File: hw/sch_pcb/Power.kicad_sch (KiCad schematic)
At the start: 32 parts

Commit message: Edit
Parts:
- removed ?: (no value), symbol Device:CP
- added C77, C79, C80: 47uF/6,3V, Mlab_R:SMD-0805, symbol Device:C
- added C81, C82: 100nF, Mlab_R:SMD-0805, symbol Device:C
- C67: renamed from ?; value (none) -> 10uF; footprint (none) -> Mlab_R:SMD-0805; Hodnota 10uF -> (none); Odkaz C31 -> (none); Pouzdro Mlab_R:SMD-0805 -> (none)
- C68: renamed from ?; value (none) -> 10uF; footprint (none) -> Mlab_R:SMD-0805; Hodnota 10uF -> (none); Odkaz C32 -> (none); Pouzdro Mlab_R:SMD-0805 -> (none)
- C69: renamed from ?; value (none) -> 100nF; footprint (none) -> Mlab_R:SMD-0805; Hodnota 100nF -> (none); Odkaz C33 -> (none); Pouzdro Mlab_R:SMD-0805 -> (none)
- C70: renamed from ?; value (none) -> 100nF; footprint (none) -> Mlab_R:SMD-0805; Hodnota 100nF -> (none); Odkaz C34 -> (none); Pouzdro Mlab_R:SMD-0805 -> (none)
- C71: renamed from ?; value (none) -> 100nF; footprint (none) -> Mlab_R:SMD-0805; Hodnota 100nF -> (none); Odkaz C35 -> (none); Pouzdro Mlab_R:SMD-0805 -> (none)
- C72: renamed from ?; value (none) -> 100nF; footprint (none) -> Mlab_R:SMD-0805; Hodnota 100nF -> (none); Odkaz C36 -> (none); Pouzdro Mlab_R:SMD-0805 -> (none)
- C73: renamed from ?; value (none) -> 10uF; footprint (none) -> Mlab_R:SMD-0805; Hodnota 10uF -> (none); Odkaz C37 -> (none); Pouzdro Mlab_R:SMD-0805 -> (none)
- C74: renamed from ?; value (none) -> 10uF; footprint (none) -> Mlab_R:SMD-0805; Hodnota 10uF -> (none); Odkaz C38 -> (none); Pouzdro Mlab_R:SMD-0805 -> (none)
- C75: renamed from ?; value (none) -> 10uF; footprint (none) -> Mlab_R:SMD-0805; Hodnota 10uF -> (none); Odkaz C39 -> (none); Pouzdro Mlab_R:SMD-0805 -> (none)
- C76: renamed from ?; value (none) -> 10uF; footprint (none) -> Mlab_R:SMD-0805; Hodnota 10uF -> (none); Odkaz C40 -> (none); Pouzdro Mlab_R:SMD-0805 -> (none)
- C78: renamed from ?; value (none) -> 47uF/16; footprint (none) -> Mlab_C:TantalC_SizeC_Reflow; Hodnota 47uF/16 -> (none); Odkaz C42 -> (none); Pouzdro Mlab_C:TantalC_SizeC_Reflow -> (none)
- D2: renamed from ?; value (none) -> RED; footprint (none) -> Mlab_D:LED_1206; Hodnota RED -> (none); Odkaz D2 -> (none); Pouzdro Mlab_D:LED_1206 -> (none)
- D3: renamed from ?; value (none) -> RED; footprint (none) -> Mlab_D:LED_1206; Hodnota RED -> (none); Odkaz D3 -> (none); Pouzdro Mlab_D:LED_1206 -> (none)
- L48: renamed from ?; value (none) -> 1uH; footprint (none) -> Mlab_L:DE1205-10; Hodnota 1uH -> (none); Odkaz L8 -> (none); Pouzdro Mlab_L:DE1205-10 -> (none)
- L49: renamed from ?; value (none) -> 1uH; footprint (none) -> Mlab_L:DE1205-10; Hodnota 1uH -> (none); Odkaz L9 -> (none); Pouzdro Mlab_L:DE1205-10 -> (none)
- L50: renamed from ?; value (none) -> BLM21PG331SN1D; Hodnota BLM21PG331SN1D -> (none); Odkaz L10 -> (none)
- L51: renamed from ?; value (none) -> BLM21PG331SN1D; Hodnota BLM21PG331SN1D -> (none); Odkaz L11 -> (none)
- R43: renamed from ?; value (none) -> 100k; footprint (none) -> Mlab_R:SMD-0805; Hodnota 100k -> (none); Odkaz R30 -> (none); Pouzdro Mlab_R:SMD-0805 -> (none)
- R44: renamed from ?; value (none) -> -; footprint (none) -> Mlab_R:SMD-0805; Hodnota - -> (none); Odkaz R31 -> (none); Pouzdro Mlab_R:SMD-0805 -> (none)
- R45: renamed from ?; value (none) -> 100k; footprint (none) -> Mlab_R:SMD-0805; Hodnota 100k -> (none); Odkaz R32 -> (none); Pouzdro Mlab_R:SMD-0805 -> (none)
- R46: renamed from ?; value (none) -> -; footprint (none) -> Mlab_R:SMD-0805; Hodnota - -> (none); Odkaz R33 -> (none); Pouzdro Mlab_R:SMD-0805 -> (none)
- R47: renamed from ?; value (none) -> 10k; footprint (none) -> Mlab_R:SMD-0805; Hodnota 10k -> (none); Odkaz R34 -> (none); Pouzdro Mlab_R:SMD-0805 -> (none)
- R48: renamed from ?; value (none) -> 10k; footprint (none) -> Mlab_R:SMD-0805; Hodnota 10k -> (none); Odkaz R35 -> (none); Pouzdro Mlab_R:SMD-0805 -> (none)
- R49: renamed from ?; value (none) -> 0R; footprint (none) -> Mlab_R:SMD-0805; Hodnota 0R -> (none); Odkaz R36 -> (none); Pouzdro Mlab_R:SMD-0805 -> (none)
- R50: renamed from ?; value (none) -> 0R; footprint (none) -> Mlab_R:SMD-0805; Hodnota 0R -> (none); Odkaz R37 -> (none); Pouzdro Mlab_R:SMD-0805 -> (none)
- R51: renamed from ?; value (none) -> 45k3; footprint (none) -> Mlab_R:SMD-0805; Hodnota 45k3 -> (none); Odkaz R38 -> (none); Pouzdro Mlab_R:SMD-0805 -> (none)
- R52: renamed from ?; value (none) -> 73k2; footprint (none) -> Mlab_R:SMD-0805; Hodnota 73k2 -> (none); Odkaz R39 -> (none); Pouzdro Mlab_R:SMD-0805 -> (none)
- R53: renamed from ?; value (none) -> 240R; footprint (none) -> Mlab_R:SMD-0805; Hodnota 240R -> (none); Odkaz R40 -> (none); Pouzdro Mlab_R:SMD-0805 -> (none)
- R54: renamed from ?; value (none) -> 240R; footprint (none) -> Mlab_R:SMD-0805; Hodnota 240R -> (none); Odkaz R41 -> (none); Pouzdro Mlab_R:SMD-0805 -> (none)
- U10: renamed from ?; value (none) -> TPS563249; footprint (none) -> Package_TO_SOT_SMD:SOT-23-6; Hodnota TPS563249 -> (none); Odkaz U6 -> (none); Pouzdro Package_TO_SOT_SMD:SOT-23-6 -> (none)
- U11: renamed from ?; value (none) -> TPS563249; footprint (none) -> Package_TO_SOT_SMD:SOT-23-6; Hodnota TPS563249 -> (none); Odkaz U7 -> (none); Pouzdro Package_TO_SOT_SMD:SOT-23-6 -> (none)
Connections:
- net +3V3: now also C79.2, C81.2
- net +5V: now also C80.2, C82.2
- net GND: now also C77.1, C79.1, C80.1, C81.1, C82.1
- net at C73.2, C75.2, L48.2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: now also C77.2

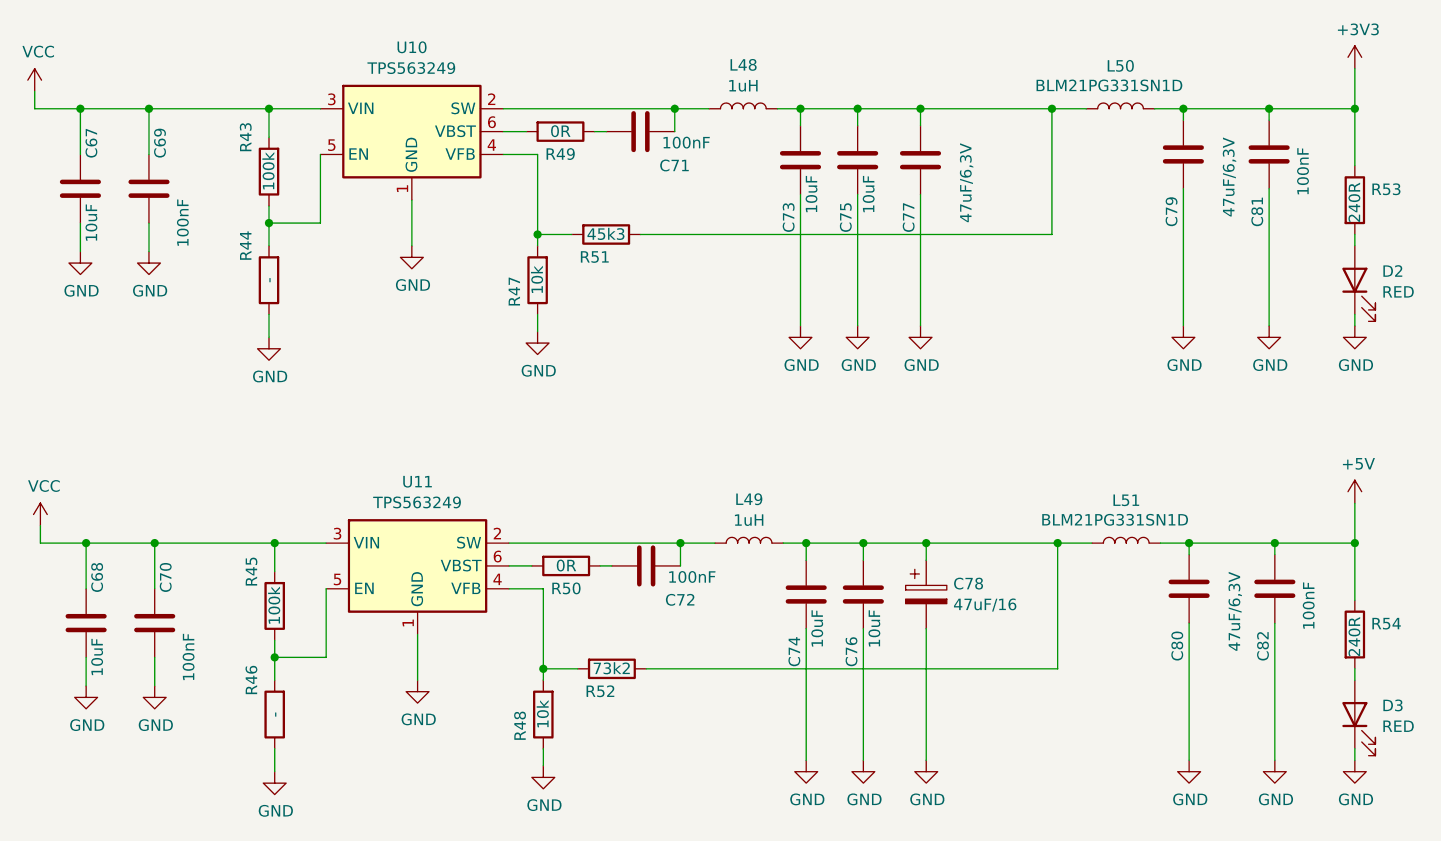
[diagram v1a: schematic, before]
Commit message: Update resistors value to increase DC gain.
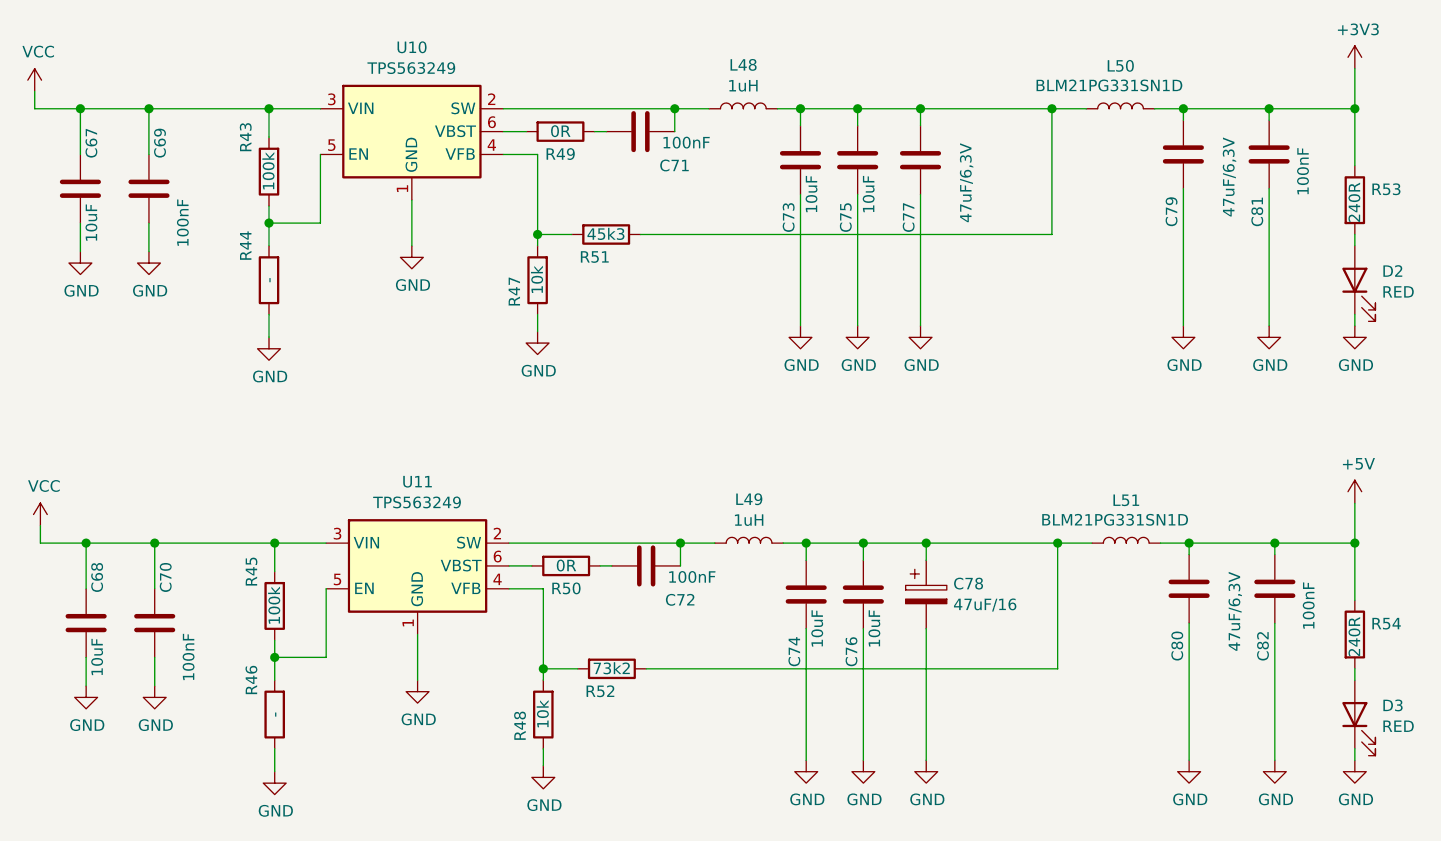
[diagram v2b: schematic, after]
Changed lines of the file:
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@@
-(kicad_sch (version 20200618) (host eeschema "(5.99.0-2251-g5226d6b4d)")
+(kicad_sch (version 20201015) (generator eeschema)
   (page 1 3)
   (paper "A4")
-  (junction (at 77.47 26.67) (diameter 0) (color 0 0 0 0))
-  (junction (at 78.105 74.93) (diameter 0) (color 0 0 0 0))
-  (junction (at 85.09 26.67) (diameter 0) (color 0 0 0 0))
-  (junction (at 85.725 74.93) (diameter 0) (color 0 0 0 0))
-  (junction (at 98.425 26.67) (diameter 0) (color 0 0 0 0))
-  (junction (at 98.425 39.37) (diameter 0) (color 0 0 0 0))
-  (junction (at 99.06 74.93) (diameter 0) (color 0 0 0 0))
-  (junction (at 99.06 87.63) (diameter 0) (color 0 0 0 0))
-  (junction (at 128.27 40.64) (diameter 0) (color 0 0 0 0))
-  (junction (at 128.905 88.9) (diameter 0) (color 0 0 0 0))
-  (junction (at 143.51 26.67) (diameter 0) (color 0 0 0 0))
-  (junction (at 144.145 74.93) (diameter 0) (color 0 0 0 0))
-  (junction (at 157.48 26.67) (diameter 0) (color 0 0 0 0))
-  (junction (at 158.115 74.93) (diameter 0) (color 0 0 0 0))
-  (junction (at 163.83 26.67) (diameter 0) (color 0 0 0 0))
-  (junction (at 164.465 74.93) (diameter 0) (color 0 0 0 0))
-  (junction (at 170.815 26.67) (diameter 0) (color 0 0 0 0))
-  (junction (at 171.45 74.93) (diameter 0) (color 0 0 0 0))
-  (junction (at 185.42 26.67) (diameter 0) (color 0 0 0 0))
-  (junction (at 186.055 74.93) (diameter 0) (color 0 0 0 0))
-  (junction (at 200.025 26.67) (diameter 0) (color 0 0 0 0))
-  (junction (at 200.66 74.93) (diameter 0) (color 0 0 0 0))
-  (junction (at 209.55 26.67) (diameter 0) (color 0 0 0 0))
-  (junction (at 210.185 74.93) (diameter 0) (color 0 0 0 0))
-  (junction (at 219.075 26.67) (diameter 0) (color 0 0 0 0))
-  (junction (at 219.075 74.93) (diameter 0) (color 0 0 0 0))
+  (junction (at 77.47 26.67) (diameter 1.016) (color 0 0 0 0))
+  (junction (at 78.105 74.93) (diameter 1.016) (color 0 0 0 0))
+  (junction (at 85.09 26.67) (diameter 1.016) (color 0 0 0 0))
+  (junction (at 85.725 74.93) (diameter 1.016) (color 0 0 0 0))
+  (junction (at 98.425 26.67) (diameter 1.016) (color 0 0 0 0))
+  (junction (at 98.425 39.37) (diameter 1.016) (color 0 0 0 0))
+  (junction (at 99.06 74.93) (diameter 1.016) (color 0 0 0 0))
+  (junction (at 99.06 87.63) (diameter 1.016) (color 0 0 0 0))
+  (junction (at 128.27 40.64) (diameter 1.016) (color 0 0 0 0))
+  (junction (at 128.905 88.9) (diameter 1.016) (color 0 0 0 0))
+  (junction (at 143.51 26.67) (diameter 1.016) (color 0 0 0 0))
+  (junction (at 144.145 74.93) (diameter 1.016) (color 0 0 0 0))
+  (junction (at 157.48 26.67) (diameter 1.016) (color 0 0 0 0))
+  (junction (at 158.115 74.93) (diameter 1.016) (color 0 0 0 0))
+  (junction (at 163.83 26.67) (diameter 1.016) (color 0 0 0 0))
+  (junction (at 164.465 74.93) (diameter 1.016) (color 0 0 0 0))
+  (junction (at 170.815 26.67) (diameter 1.016) (color 0 0 0 0))
+  (junction (at 171.45 74.93) (diameter 1.016) (color 0 0 0 0))
+  (junction (at 185.42 26.67) (diameter 1.016) (color 0 0 0 0))
+  (junction (at 186.055 74.93) (diameter 1.016) (color 0 0 0 0))
+  (junction (at 200.025 26.67) (diameter 1.016) (color 0 0 0 0))
+  (junction (at 200.66 74.93) (diameter 1.016) (color 0 0 0 0))
+  (junction (at 209.55 26.67) (diameter 1.016) (color 0 0 0 0))
+  (junction (at 210.185 74.93) (diameter 1.016) (color 0 0 0 0))
+  (junction (at 219.075 26.67) (diameter 1.016) (color 0 0 0 0))
+  (junction (at 219.075 74.93) (diameter 1.016) (color 0 0 0 0))
   (wire (pts (xy 72.39 24.765) (xy 72.39 26.67))
     (stroke (width 0) (type solid) (color 0 0 0 0))

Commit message: edit
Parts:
- C67, C68, C73, C74, C75, C76: value 10uF -> 10uF/16; footprint Mlab_R:SMD-0805 -> Capacitor_SMD:C_0805_2012Metric; UST_ID 5c70984812875079b91f8bbe -> (none)
- C69, C70, C71, C72, C81, C82: footprint Mlab_R:SMD-0805 -> Mlab_C:SMD-0603
- C77, C79, C80: footprint Mlab_R:SMD-0805 -> Capacitor_SMD:C_0805_2012Metric
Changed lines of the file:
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@@
     (in_bom yes) (on_board yes)
     (property "Reference" "C67" (id 0) (at 78.74 30.48 90))
-    (property "Value" "10uF" (id 1) (at 78.74 39.37 90))
-    (property "Footprint" "Mlab_R:SMD-0805" (id 2) (at 76.5048 31.75 0)
+    (property "Value" "10uF/16" (id 1) (at 78.74 39.37 90))
+    (property "Footprint" "Capacitor_SMD:C_0805_2012Metric" (id 2) (at 76.5048 31.75 0)
       (effects (font (size 1.27 1.27)) hide)
     )
@@
       (effects (font (size 1.27 1.27)) hide)
     )
-    (property "UST_ID" "5c70984812875079b91f8bbe" (id 4) (at 77.47 35.56 0)
+    (property "UST_ID" "" (id 4) (at 77.47 35.56 0)
       (effects (font (size 1.27 1.27)) hide)
     )
@@
     (in_bom yes) (on_board yes)
     (property "Reference" "C68" (id 0) (at 79.375 78.74 90))
-    (property "Value" "10uF" (id 1) (at 79.375 87.63 90))
-    (property "Footprint" "Mlab_R:SMD-0805" (id 2) (at 77.1398 80.01 0)
+    (property "Value" "10uF/16" (id 1) (at 79.375 87.63 90))
+    (property "Footprint" "Capacitor_SMD:C_0805_2012Metric" (id 2) (at 77.1398 80.01 0)
       (effects (font (size 1.27 1.27)) hide)
     )
@@
       (effects (font (size 1.27 1.27)) hide)
     )
-    (property "UST_ID" "5c70984812875079b91f8bbe" (id 4) (at 78.105 83.82 0)
+    (property "UST_ID" "" (id 4) (at 78.105 83.82 0)
       (effects (font (size 1.27 1.27)) hide)
     )
@@
     (property "Reference" "C69" (id 0) (at 86.36 30.48 90))
     (property "Value" "100nF" (id 1) (at 88.9 39.37 90))
-    (property "Footprint" "Mlab_R:SMD-0805" (id 2) (at 84.1248 31.75 0)
+    (property "Footprint" "Mlab_C:SMD-0603" (id 2) (at 84.1248 31.75 0)
       (effects (font (size 1.27 1.27)) hide)
     )
@@
     (property "Reference" "C70" (id 0) (at 86.995 78.74 90))
     (property "Value" "100nF" (id 1) (at 89.535 87.63 90))
-    (property "Footprint" "Mlab_R:SMD-0805" (id 2) (at 84.7598 80.01 0)
+    (property "Footprint" "Mlab_C:SMD-0603" (id 2) (at 84.7598 80.01 0)
       (effects (font (size 1.27 1.27)) hide)
     )
@@
     (property "Reference" "C71" (id 0) (at 143.51 33.02 90))
     (property "Value" "100nF" (id 1) (at 144.78 30.48 90))
-    (property "Footprint" "Mlab_R:SMD-0805" (id 2) (at 135.89 30.1752 0)
+    (property "Footprint" "Mlab_C:SMD-0603" (id 2) (at 135.89 30.1752 0)
       (effects (font (size 1.27 1.27)) hide)
     )
@@
     (property "Reference" "C72" (id 0) (at 144.145 81.28 90))
     (property "Value" "100nF" (id 1) (at 145.415 78.74 90))
-    (property "Footprint" "Mlab_R:SMD-0805" (id 2) (at 136.525 78.4352 0)
+    (property "Footprint" "Mlab_C:SMD-0603" (id 2) (at 136.525 78.4352 0)
       (effects (font (size 1.27 1.27)) hide)
     )
@@
     (in_bom yes) (on_board yes)
     (property "Reference" "C73" (id 0) (at 156.21 38.735 90))
-    (property "Value" "10uF" (id 1) (at 158.75 36.195 90))
-    (property "Footprint" "Mlab_R:SMD-0805" (id 2) (at 156.5148 28.575 0)
+    (property "Value" "10uF/16" (id 1) (at 158.75 36.195 90))
+    (property "Footprint" "Capacitor_SMD:C_0805_2012Metric" (id 2) (at 156.5148 28.575 0)
       (effects (font (size 1.27 1.27)) hide)
     )
@@
       (effects (font (size 1.27 1.27)) hide)
     )
-    (property "UST_ID" "5c70984812875079b91f8bbe" (id 4) (at 157.48 32.385 0)
+    (property "UST_ID" "" (id 4) (at 157.48 32.385 0)
       (effects (font (size 1.27 1.27)) hide)
     )
@@
     (in_bom yes) (on_board yes)
     (property "Reference" "C74" (id 0) (at 156.845 86.995 90))
-    (property "Value" "10uF" (id 1) (at 159.385 84.455 90))
-    (property "Footprint" "Mlab_R:SMD-0805" (id 2) (at 157.1498 76.835 0)
+    (property "Value" "10uF/16" (id 1) (at 159.385 84.455 90))
+    (property "Footprint" "Capacitor_SMD:C_0805_2012Metric" (id 2) (at 157.1498 76.835 0)
       (effects (font (size 1.27 1.27)) hide)
     )
@@
       (effects (font (size 1.27 1.27)) hide)
     )
-    (property "UST_ID" "5c70984812875079b91f8bbe" (id 4) (at 158.115 80.645 0)
+    (property "UST_ID" "" (id 4) (at 158.115 80.645 0)
       (effects (font (size 1.27 1.27)) hide)
     )
@@
     (in_bom yes) (on_board yes)
     (property "Reference" "C75" (id 0) (at 162.56 38.735 90))
-    (property "Value" "10uF" (id 1) (at 165.1 36.195 90))
-    (property "Footprint" "Mlab_R:SMD-0805" (id 2) (at 162.8648 28.575 0)
+    (property "Value" "10uF/16" (id 1) (at 165.1 36.195 90))
+    (property "Footprint" "Capacitor_SMD:C_0805_2012Metric" (id 2) (at 162.8648 28.575 0)
       (effects (font (size 1.27 1.27)) hide)
     )
@@
       (effects (font (size 1.27 1.27)) hide)
     )
-    (property "UST_ID" "5c70984812875079b91f8bbe" (id 4) (at 163.83 32.385 0)
+    (property "UST_ID" "" (id 4) (at 163.83 32.385 0)
       (effects (font (size 1.27 1.27)) hide)
     )
@@
     (in_bom yes) (on_board yes)
     (property "Reference" "C76" (id 0) (at 163.195 86.995 90))
-    (property "Value" "10uF" (id 1) (at 165.735 84.455 90))
-    (property "Footprint" "Mlab_R:SMD-0805" (id 2) (at 163.4998 76.835 0)
+    (property "Value" "10uF/16" (id 1) (at 165.735 84.455 90))
+    (property "Footprint" "Capacitor_SMD:C_0805_2012Metric" (id 2) (at 163.4998 76.835 0)
       (effects (font (size 1.27 1.27)) hide)
     )
@@
       (effects (font (size 1.27 1.27)) hide)
     )
-    (property "UST_ID" "5c70984812875079b91f8bbe" (id 4) (at 164.465 80.645 0)
+    (property "UST_ID" "" (id 4) (at 164.465 80.645 0)
       (effects (font (size 1.27 1.27)) hide)
     )
@@
     (property "Reference" "C77" (id 0) (at 169.545 38.735 90))
     (property "Value" "47uF/6,3V" (id 1) (at 175.895 34.925 90))
-    (property "Footprint" "Mlab_R:SMD-0805" (id 2) (at 169.8498 28.575 0)
+    (property "Footprint" "Capacitor_SMD:C_0805_2012Metric" (id 2) (at 169.8498 28.575 0)
       (effects (font (size 1.27 1.27)) hide)
     )
@@
     (property "Reference" "C79" (id 0) (at 198.755 38.1 90))
     (property "Value" "47uF/6,3V" (id 1) (at 205.105 34.29 90))
-    (property "Footprint" "Mlab_R:SMD-0805" (id 2) (at 199.0598 27.94 0)
+    (property "Footprint" "Capacitor_SMD:C_0805_2012Metric" (id 2) (at 199.0598 27.94 0)
       (effects (font (size 1.27 1.27)) hide)
     )
@@
     (property "Reference" "C80" (id 0) (at 199.39 86.36 90))
     (property "Value" "47uF/6,3V" (id 1) (at 205.74 82.55 90))
-    (property "Footprint" "Mlab_R:SMD-0805" (id 2) (at 199.6948 76.2 0)
+    (property "Footprint" "Capacitor_SMD:C_0805_2012Metric" (id 2) (at 199.6948 76.2 0)
       (effects (font (size 1.27 1.27)) hide)
     )
@@
     (property "Reference" "C81" (id 0) (at 208.28 38.1 90))
     (property "Value" "100nF" (id 1) (at 213.36 33.655 90))
-    (property "Footprint" "Mlab_R:SMD-0805" (id 2) (at 208.5848 27.94 0)
+    (property "Footprint" "Mlab_C:SMD-0603" (id 2) (at 208.5848 27.94 0)
       (effects (font (size 1.27 1.27)) hide)
     )
@@
     (property "Reference" "C82" (id 0) (at 208.915 86.36 90))
     (property "Value" "100nF" (id 1) (at 213.995 81.915 90))
-    (property "Footprint" "Mlab_R:SMD-0805" (id 2) (at 209.2198 76.2 0)
-      (effects (font (size 1.27 1.27)) hide)
-    )
+    (property "Footprint" "Mlab_C:SMD-0603" (id 2) (at 209.2198 76.2 0)
+      (effects (font (size 1.27 1.27)) hide)
+    )

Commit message: Edit pouzdra
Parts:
- L50, L51: footprint (none) -> Mlab_R:SMD-0805
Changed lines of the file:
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@@
     (property "Reference" "L50" (id 0) (at 193.04 21.9518 90))
     (property "Value" "BLM21PG331SN1D" (id 1) (at 191.77 24.13 90))
-    (property "Footprint" "" (id 2) (at 193.04 26.67 0)
+    (property "Footprint" "Mlab_R:SMD-0805" (id 2) (at 193.04 26.67 0)
       (effects (font (size 1.27 1.27)) hide)
     )
@@
     (property "Reference" "L51" (id 0) (at 193.675 70.2118 90))
     (property "Value" "BLM21PG331SN1D" (id 1) (at 192.405 72.39 90))
-    (property "Footprint" "" (id 2) (at 193.675 74.93 0)
+    (property "Footprint" "Mlab_R:SMD-0805" (id 2) (at 193.675 74.93 0)
       (effects (font (size 1.27 1.27)) hide)
     )
